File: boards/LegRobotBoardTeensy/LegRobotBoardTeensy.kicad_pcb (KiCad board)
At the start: 2 copper layers, 109.6 x 116.6 mm, 116 parts, among them J1 IDC, J10 IDC, J11 IDC, J12 IDC, J13 IDC, J14 IDC, J15 IDC, J16 IDC, J2 B3B-XH-A, J3 B3B-XH-A, J4 B3B-XH-A, J5 B3B-XH-A, J6 IDC, J7 IDC, J8 IDC, J9 IDC, Q1 MMBT3904LT1G, Q10 MMBT3904LT1G, Q11 MMBT3904LT1G, Q12 MMBT3904LT1G, Q13 MMBT3904LT1G, Q14 MMBT3904LT1G, Q15 MMBT3904LT1G, Q16 MMBT3904LT1G, Q17 MMBT3904LT1G, Q18 MMBT3904LT1G, Q19 MMBT3904LT1G, Q2 MMBT3904LT1G, Q20 MMBT3904LT1G, Q21 MMBT3904LT1G, Q22 MMBT3904LT1G, Q23 MMBT3904LT1G, Q24 MMBT3904LT1G, Q3 MMBT3904LT1G, Q4 MMBT3904LT1G, Q5 MMBT3904LT1G, Q6 MMBT3904LT1G, Q7 MMBT3904LT1G, Q8 MMBT3904LT1G, Q9 MMBT3904LT1G, U1 Teensy4.0, U2 TLC555CDR, U3 SN74HC08DR, U4 SN74HC08DR, U5 PCA9685PW_118, U6 SN74HC08DR, U7 SN74HC08DR, U8 BNO055

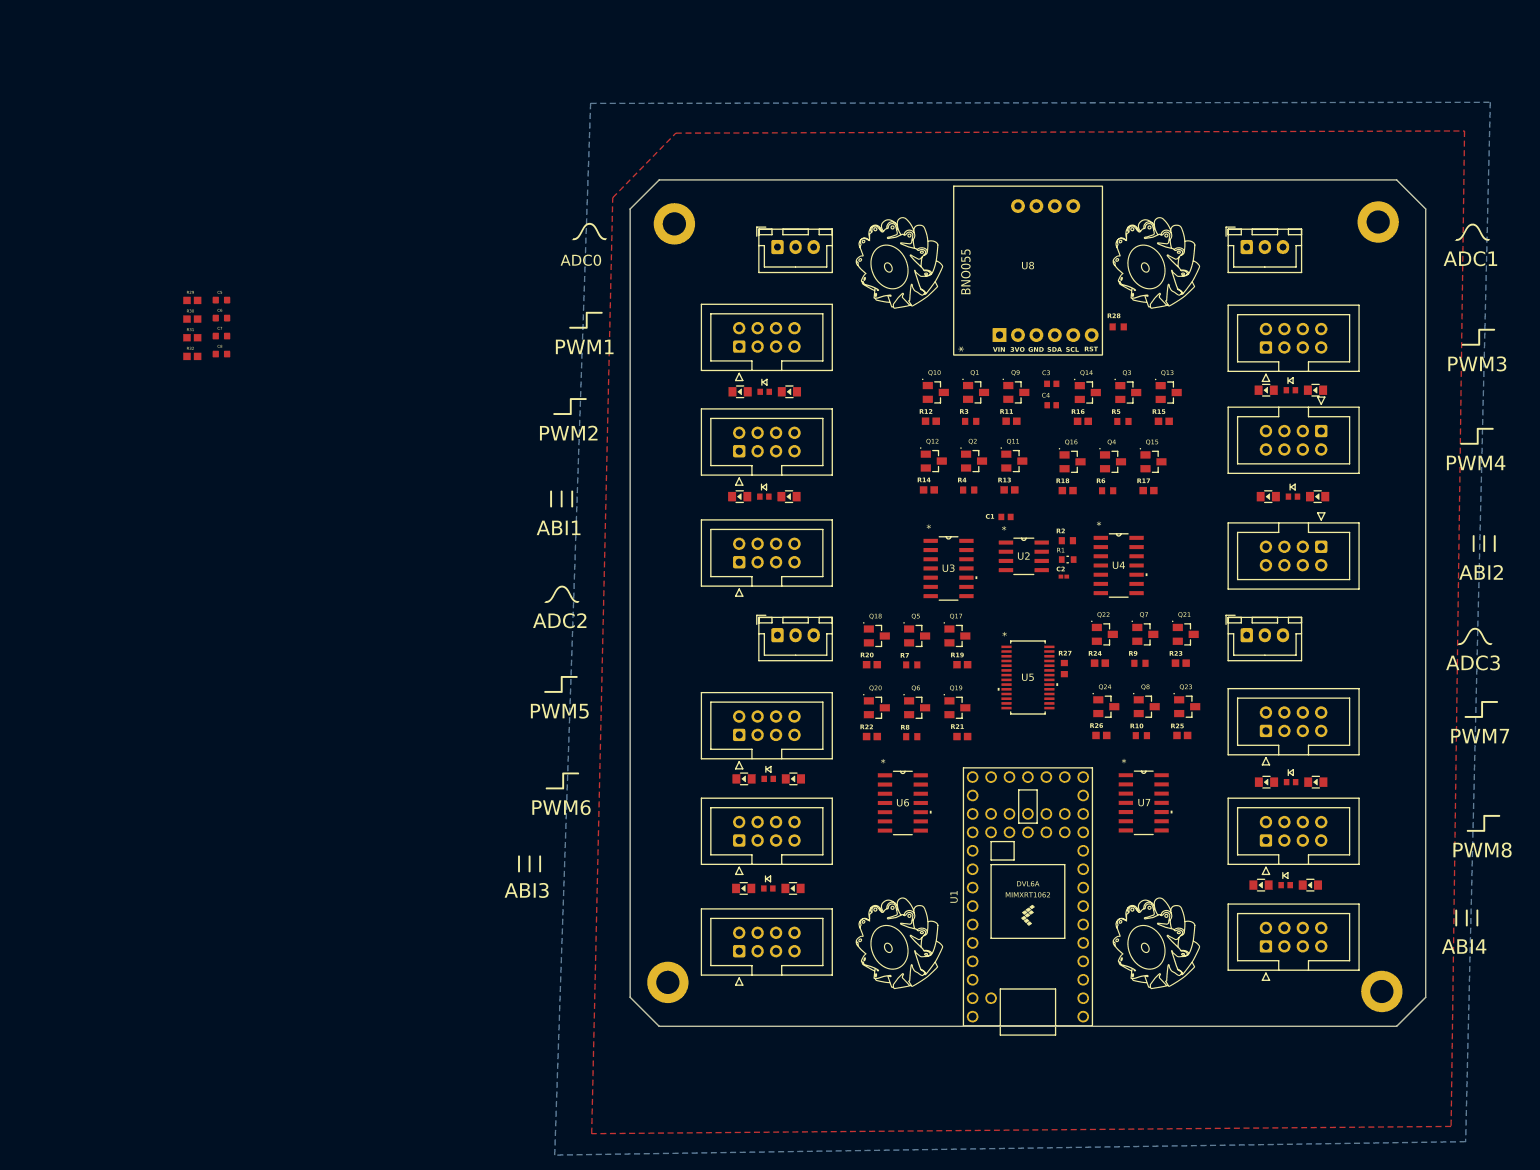
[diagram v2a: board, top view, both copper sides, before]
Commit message: Debug and re-design leg encoder and leg robot board
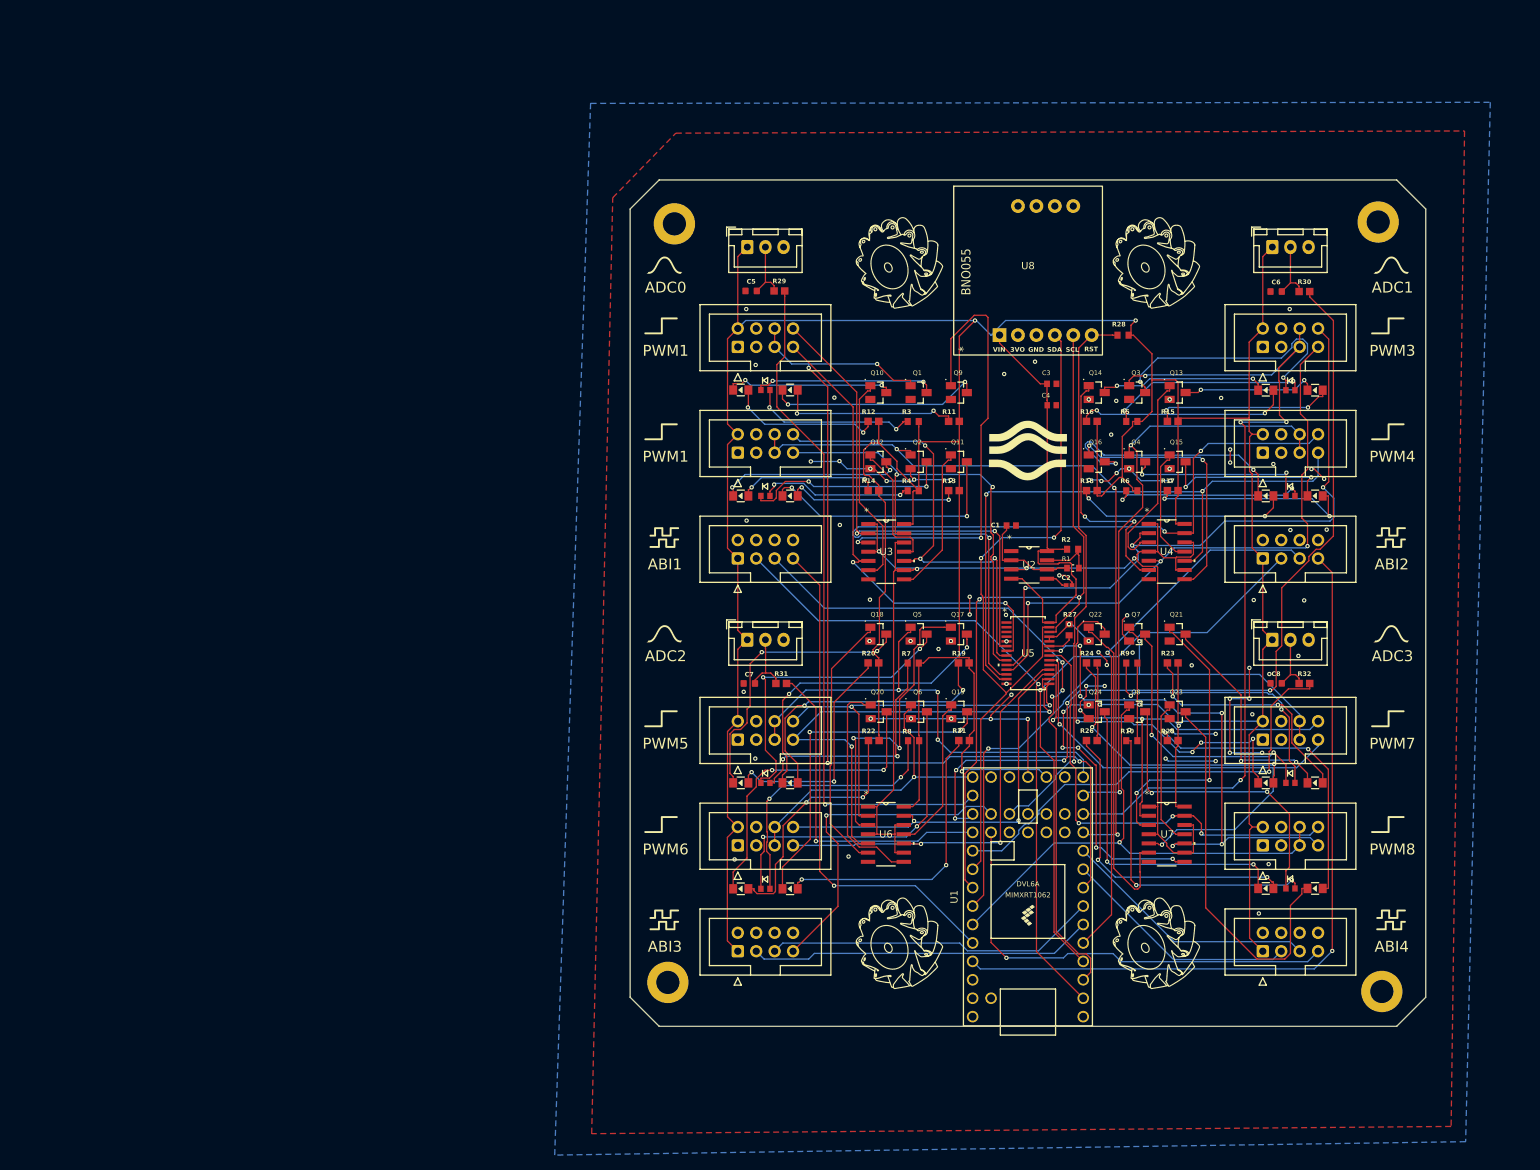
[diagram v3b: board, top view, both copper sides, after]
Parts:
- moved R32 159.8 mm to (186.2, 99.6)
- moved R30 153.3 mm to (186.2, 45.6)
- moved C8 152.3 mm to (182.3, 99.6)
- moved C6 145.4 mm to (182.3, 45.6)
- moved R31 94.1 mm to (114.1, 99.6)
- moved C7 87.1 mm to (109.7, 99.6)
- moved R29 80.9 mm to (113.9, 45.5)
- moved C5 73.0 mm to (110.0, 45.5)
- moved U3 8.89 mm to (128.6, 81.4)
- moved J9 8.59 mm to (180.5, 67.8), turned to 90 degrees
- moved J14 8.21 mm to (180.5, 82.4), turned to 90 degrees
- moved Q1 7.92 mm to (133.1, 59.5)
- moved Q10 7.92 mm to (127.5, 59.5)
- moved Q9 7.92 mm to (138.6, 59.5)
- moved R11 7.92 mm to (137.9, 63.5)
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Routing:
- net +3.3V: track 0.00 -> 659.3 mm, vias 0 -> 6
- net BLINK: track 0.00 -> 176.5 mm, vias 0 -> 4
- net PWMEN1: track 0.00 -> 134.3 mm, vias 0 -> 4
- net GND: track 0.00 -> 133.7 mm, vias 0 -> 79
- net A1: track 0.00 -> 122.0 mm, vias 0 -> 5
- net PWMEN3: track 0.00 -> 120.4 mm, vias 0 -> 4
- net RPWM4: track 0.00 -> 116.6 mm, vias 0 -> 3
- net PWMEN2: track 0.00 -> 107.7 mm, vias 0 -> 3
- net ENCODER2_I: track 0.00 -> 105.9 mm, vias 0 -> 1
- net SCL: track 0.00 -> 98.9 mm, vias 0 -> 2
- net SDA: track 0.00 -> 98.2 mm, vias 0 -> 2
- net A0: track 0.00 -> 94.8 mm, vias 0 -> 1
- net ENCODER1_B: track 0.00 -> 94.4 mm, vias 0 -> 3
- net ENCODER1_A: track 0.00 -> 92.1 mm, vias 0 -> 1
- net RPWM3: track 0.00 -> 92.0 mm, vias 0 -> 3
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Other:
- board text removed: "PWM2"

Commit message: Clean up and document boards
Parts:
- moved MH3 65.5 mm to (45.6, 102.2)
- moved Q5 63.2 mm to (73.8, 114.9)
- moved Q17 63.2 mm to (79.3, 114.9)
- moved Q18 63.2 mm to (68.2, 114.9)
- moved R20 63.2 mm to (67.6, 118.9)
- moved R7 63.2 mm to (73.1, 118.9)
- moved R19 63.2 mm to (80.0, 118.9)
- moved Q1 61.5 mm to (72.4, 69.8)
- moved Q10 61.5 mm to (66.8, 69.8)
- moved R12 61.5 mm to (66.2, 73.8)
- moved Q9 61.5 mm to (78.0, 69.8)
- moved R11 61.5 mm to (77.3, 73.8)
- moved R3 61.5 mm to (71.7, 73.8)
- moved MH1 57.3 mm to (45.5, 55.6)
- moved J14 55.5 mm to (142.4, 42.0)
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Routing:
- net +3.3V: track 659.3 -> 0.00 mm, vias 6 -> 0
- net BLINK: track 176.5 -> 0.00 mm, vias 4 -> 0
- net PWMEN1: track 134.3 -> 0.00 mm, vias 4 -> 0
- net GND: track 133.7 -> 0.00 mm, vias 79 -> 0
- net A1: track 122.0 -> 0.00 mm, vias 5 -> 0
- net PWMEN3: track 120.4 -> 0.00 mm, vias 4 -> 0
- net RPWM4: track 116.6 -> 0.00 mm, vias 3 -> 0
- net PWMEN2: track 107.7 -> 0.00 mm, vias 3 -> 0
- net ENCODER2_I: track 105.9 -> 0.00 mm, vias 1 -> 0
- net SCL: track 98.9 -> 0.00 mm, vias 2 -> 0
- net SDA: track 98.2 -> 0.00 mm, vias 2 -> 0
- net A0: track 94.8 -> 0.00 mm, vias 1 -> 0
- net ENCODER1_B: track 94.4 -> 0.00 mm, vias 3 -> 0
- net ENCODER1_A: track 92.1 -> 0.00 mm, vias 1 -> 0
- net RPWM3: track 92.0 -> 0.00 mm, vias 3 -> 0
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- removed copper zone on B.Cu, net GND
- removed copper zone on F.Cu, net GND
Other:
- board size 109.6 x 116.6 mm -> 169.2 x 91.1 mm
- board text added: "PWM2"
